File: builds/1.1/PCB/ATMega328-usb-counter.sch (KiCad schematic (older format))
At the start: 38 parts, among them J1 power, J2 PROG, J3 USB_B_Micro, J4 RF, J5 PROG, Q1 MMBT3904, U1 FT230XS, U2 ATmega328PB-AU, U3 74LV8154, X1 TCXO

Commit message: rev 1.1 PCB
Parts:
- added H1, H2, H3: MountingHole, MountingHole:MountingHole_4.3mm_M4_Pad_Via, symbol Mechanical:MountingHole
- J3: footprint (none) -> Connector_USB:USB_Micro-B_Molex-105017-0001
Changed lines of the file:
@@
 F 0 "J3" H 1307 2267 50  0000 C CNN
 F 1 "USB_B_Micro" H 1307 2176 50  0000 C CNN
-F 2 "" H 1400 1750 50  0001 C CNN
+F 2 "Connector_USB:USB_Micro-B_Molex-105017-0001" H 1400 1750 50  0001 C CNN
 F 3 "~" H 1400 1750 50  0001 C CNN
 	1    1250 1800
@@
 Text Notes 9700 850  0    98   ~ 0
 LCD
+$Comp
+L Mechanical:MountingHole H1
+U 1 1 5D44527F
+P 10050 2550
+F 0 "H1" H 10150 2596 50  0000 L CNN
+F 1 "MountingHole" H 10150 2505 50  0000 L CNN
+F 2 "MountingHole:MountingHole_4.3mm_M4_Pad_Via" H 10050 2550 50  0001 C CNN
+F 3 "~" H 10050 2550 50  0001 C CNN
+	1    10050 2550
+	1    0    0    -1
+$EndComp
+$Comp
+L Mechanical:MountingHole H2
+U 1 1 5D4460C1
+P 10050 2850
+F 0 "H2" H 10150 2896 50  0000 L CNN
+F 1 "MountingHole" H 10150 2805 50  0000 L CNN
+F 2 "MountingHole:MountingHole_4.3mm_M4_Pad_Via" H 10050 2850 50  0001 C CNN
+F 3 "~" H 10050 2850 50  0001 C CNN
+	1    10050 2850
+	1    0    0    -1
+$EndComp
+$Comp
+L Mechanical:MountingHole H3
+U 1 1 5D463B97
+P 10050 3150
+F 0 "H3" H 10150 3196 50  0000 L CNN
+F 1 "MountingHole" H 10150 3105 50  0000 L CNN
+F 2 "MountingHole:MountingHole_4.3mm_M4_Pad_Via" H 10050 3150 50  0001 C CNN
+F 3 "~" H 10050 3150 50  0001 C CNN
+	1    10050 3150
+	1    0    0    -1
+$EndComp
 $EndSCHEMATC

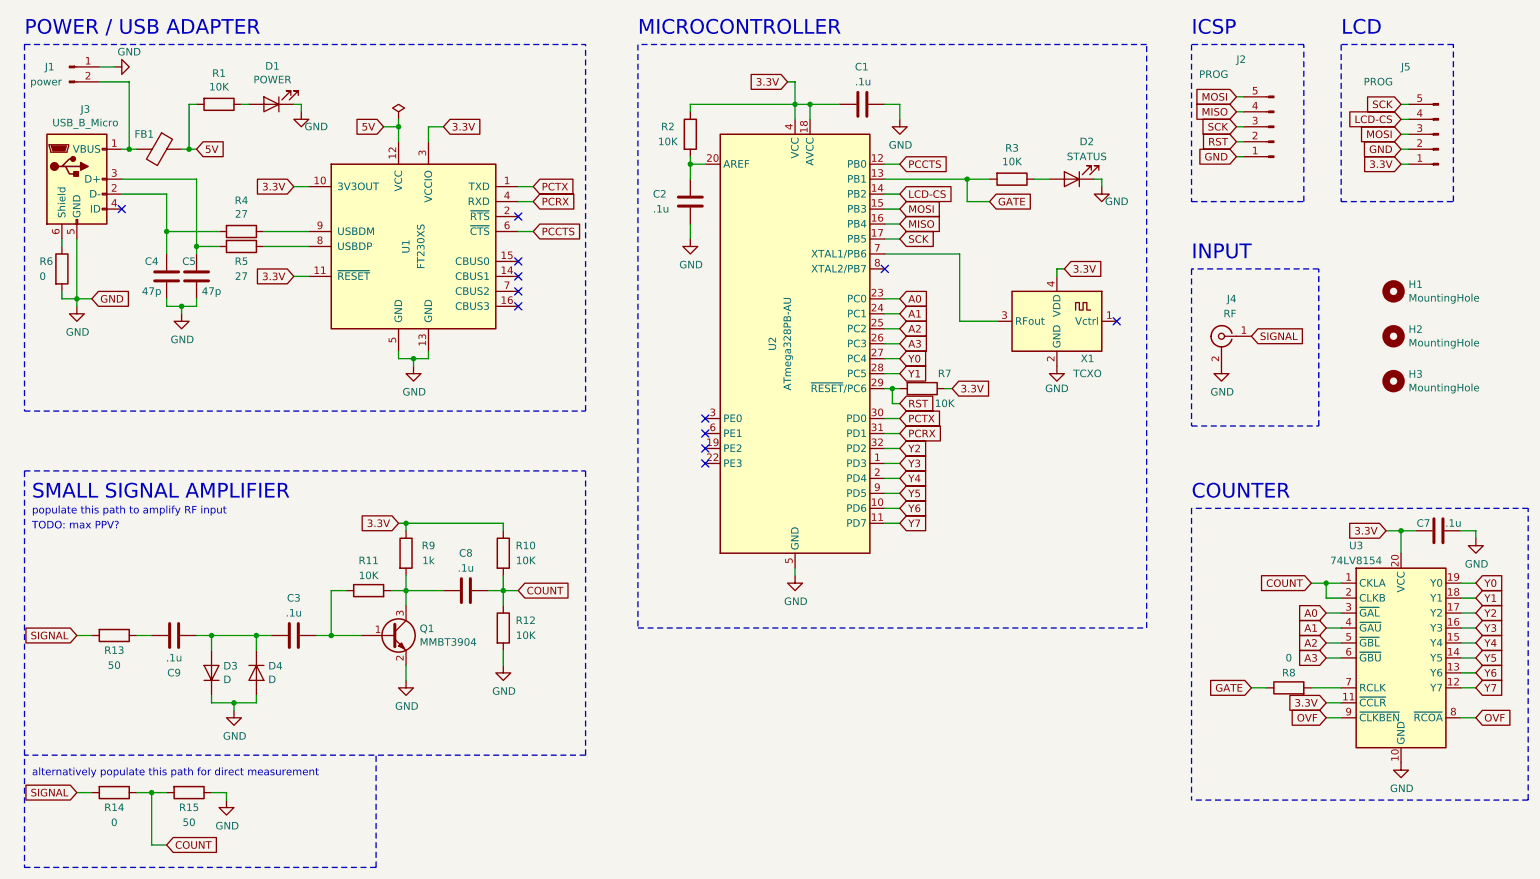
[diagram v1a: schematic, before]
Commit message: added screw hole
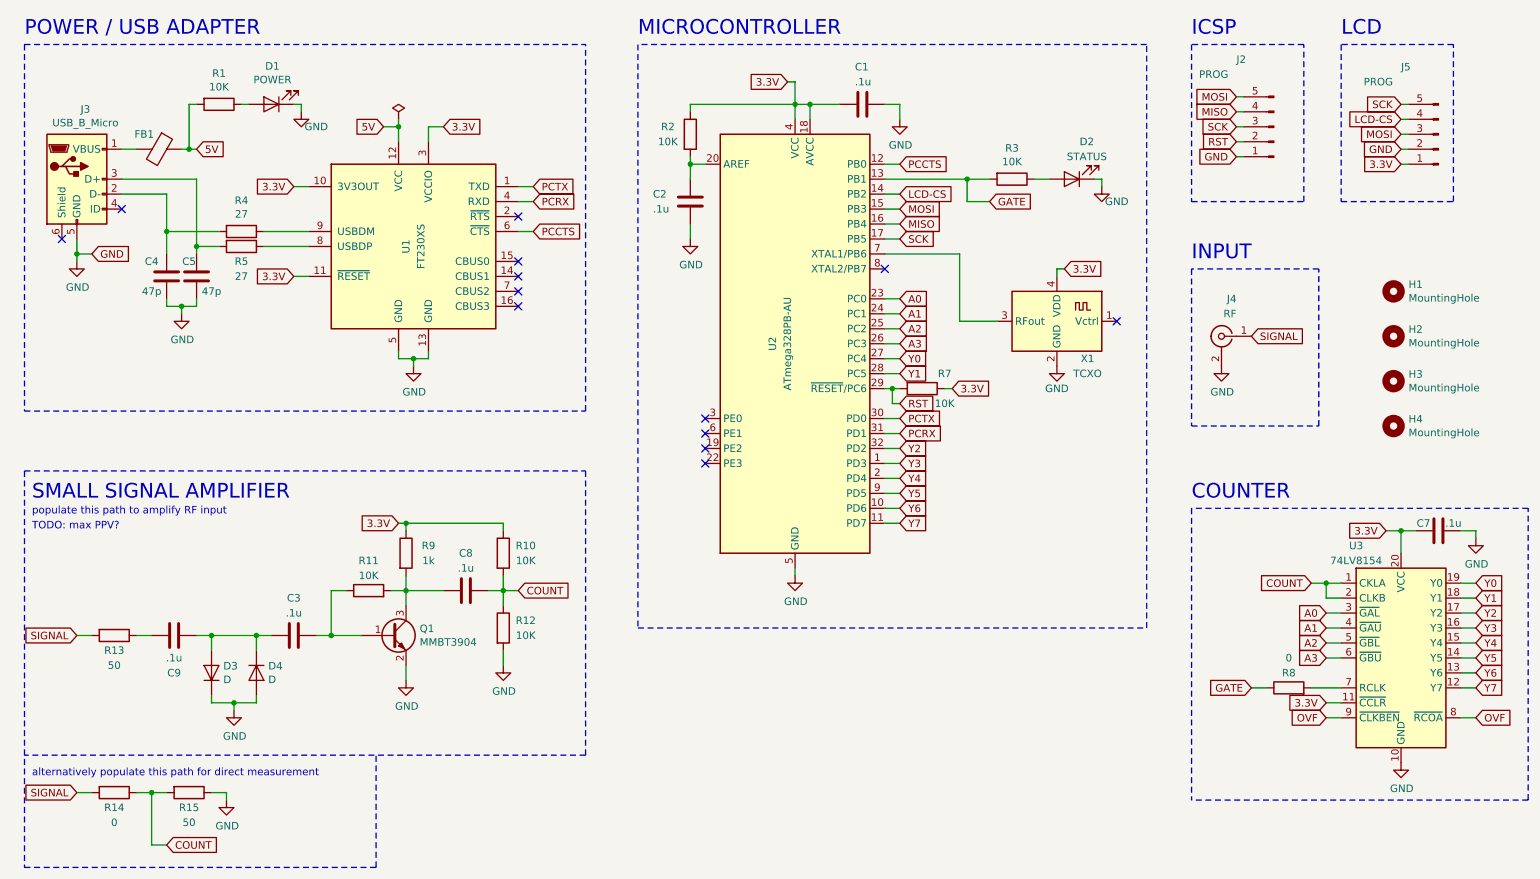
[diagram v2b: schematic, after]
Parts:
- removed J1: power, Connector_PinHeader_2.54mm:PinHeader_1x02_P2.54mm_Vertical, symbol Connector:Conn_01x02_Male
- removed R6: 0, Resistor_SMD:R_0805_2012Metric_Pad1.15x1.40mm_HandSolder, symbol Device:R
- added H4: MountingHole, MountingHole:MountingHole_4.3mm_M4_Pad_Via, symbol Mechanical:MountingHole
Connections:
- no-connect marks 12 -> 13
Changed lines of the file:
@@
 L power:GND #PWR08
 U 1 1 5CDBD712
-P 1250 2650
-F 0 "#PWR08" H 1250 2400 50  0001 C CNN
-F 1 "GND" H 1255 2477 50  0000 C CNN
-F 2 "" H 1250 2650 50  0001 C CNN
-F 3 "" H 1250 2650 50  0001 C CNN
-	1    1250 2650
-	1    0    0    -1
-$EndComp
-Wire Wire Line
-	1150 2200 1150 2250
-Wire Wire Line
-	1150 2550 1150 2600
-Wire Wire Line
-	1250 2600 1250 2200
-Wire Wire Line
-	1150 2600 1250 2600
-Wire Wire Line
-	1250 2600 1250 2650
-Connection ~ 1250 2600
+P 1250 2350
+F 0 "#PWR08" H 1250 2100 50  0001 C CNN
+F 1 "GND" H 1255 2177 50  0000 C CNN
+F 2 "" H 1250 2350 50  0001 C CNN
+F 3 "" H 1250 2350 50  0001 C CNN
+	1    1250 2350
+	1    0    0    -1
+$EndComp
+Wire Wire Line
+	1250 2300 1250 2350
 Wire Wire Line
 	2050 2250 2200 2250
@@
 	1950 2650 2050 2650
 $Comp
-L Device:R R6
-U 1 1 5CDD40A1
-P 1150 2400
-F 0 "R6" H 1000 2450 50  0000 L CNN
-F 1 "0" H 1000 2350 50  0000 L CNN
-F 2 "Resistor_SMD:R_0805_2012Metric_Pad1.15x1.40mm_HandSolder" V 1080 2400 50  0001 C CNN
-F 3 "~" H 1150 2400 50  0001 C CNN
-	1    1150 2400
-	1    0    0    -1
-$EndComp
-$Comp
 L Device:R R4
 U 1 1 5CE26301
@@
 Wire Wire Line
 	2750 1350 2750 1300
-Wire Wire Line
-	1600 1600 1550 1600
-Connection ~ 1600 1600
 Text GLabel 2050 1600 2    50   Input ~ 0
 5V
 Wire Wire Line
 	1950 1600 2000 1600
-Wire Wire Line
-	1650 1600 1600 1600
 $Comp
 L power:GND #PWR02
@@
 Wire Wire Line
 	6750 4000 6650 4000
-$Comp
-L Connector:Conn_01x02_Male J1
-U 1 1 5D39A20E
-P 1200 1050
-F 0 "J1" H 1100 1050 50  0000 R CNN
-F 1 "power" H 1150 950 50  0000 R CNN
-F 2 "Connector_PinHeader_2.54mm:PinHeader_1x02_P2.54mm_Vertical" H 1200 1050 50  0001 C CNN
-F 3 "~" H 1200 1050 50  0001 C CNN
-	1    1200 1050
-	1    0    0    -1
-$EndComp
 Text GLabel 7350 1950 2    50   Input ~ 0
 GATE
@@
 	1    0    0    -1
 $EndComp
-Wire Wire Line
-	1600 1150 1400 1150
-$Comp
-L power:GND #PWR01
-U 1 1 5D23D013
-P 1500 1050
-F 0 "#PWR01" H 1500 800 50  0001 C CNN
-F 1 "GND" V 1600 950 50  0000 C CNN
-F 2 "" H 1500 1050 50  0001 C CNN
-F 3 "" H 1500 1050 50  0001 C CNN
-	1    1500 1050
-	0    -1   -1   0
-$EndComp
-Wire Wire Line
-	1500 1050 1400 1050
 Text GLabel 6750 1700 2    50   Input ~ 0
 PCCTS
@@
 	1    0    0    -1
 $EndComp
-Wire Wire Line
-	1600 1150 1600 1600
 Wire Wire Line
 	2050 1300 2000 1300
@@
 Wire Notes Line
 	8400 4800 8400 900
-Text GLabel 1350 2600 2    50   Input ~ 0
+Text GLabel 1350 2300 2    50   Input ~ 0
 GND
 Wire Wire Line
-	1350 2600 1250 2600
+	1350 2300 1250 2300
 Text GLabel 9000 1650 0    50   Input ~ 0
 GND
@@
 	1    0    0    -1
 $EndComp
+$Comp
+L Mechanical:MountingHole H4
+U 1 1 5D3E5B2C
+P 10050 3450
+F 0 "H4" H 10150 3496 50  0000 L CNN
+F 1 "MountingHole" H 10150 3405 50  0000 L CNN
+F 2 "MountingHole:MountingHole_4.3mm_M4_Pad_Via" H 10050 3450 50  0001 C CNN
+F 3 "~" H 10050 3450 50  0001 C CNN
+	1    10050 3450
+	1    0    0    -1
+$EndComp
+Wire Wire Line
+	1550 1600 1650 1600
+Wire Wire Line
+	1250 2300 1250 2200
+Connection ~ 1250 2300
+NoConn ~ 1150 2200
 $EndSCHEMATC

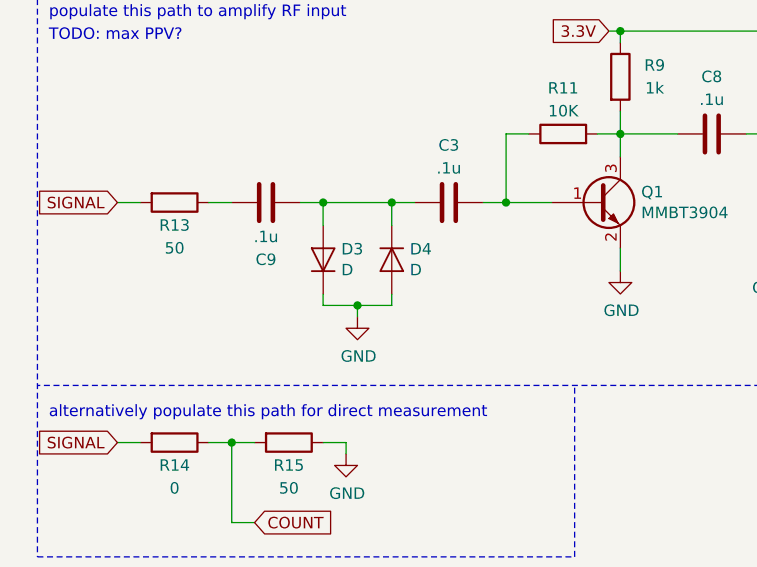
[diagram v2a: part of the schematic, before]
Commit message: new diode protection
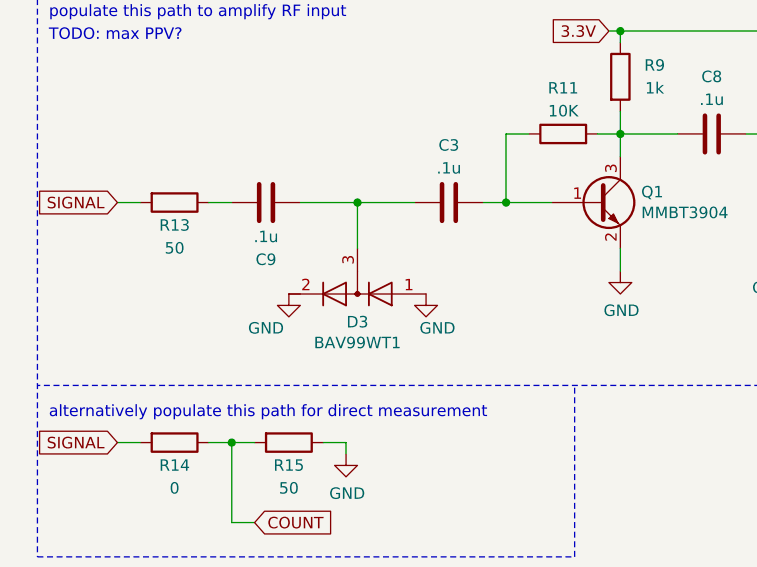
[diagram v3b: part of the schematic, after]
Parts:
- removed D3, D4: D, Diode_SMD:D_0805_2012Metric_Pad1.15x1.40mm_HandSolder, symbol Device:D
- added D3: BAV99WT1, Package_TO_SOT_SMD:SOT-323_SC-70_Handsoldering, symbol Device:D_x2_Serial_AKC
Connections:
- net GND: now also D3.1 (A), D3.2 (K)
- net at C3.2, C9.2: now also D3.3 (common)
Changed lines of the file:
@@
 	1250 4850 1350 4850
-$Comp
-L Device:D D3
-U 1 1 5D5548F3
-P 2150 5100
-F 0 "D3" V 2196 5021 50  0000 R CNN
-F 1 "D" V 2105 5021 50  0000 R CNN
-F 2 "Diode_SMD:D_0805_2012Metric_Pad1.15x1.40mm_HandSolder" H 2150 5100 50  0001 C CNN
-F 3 "~" H 2150 5100 50  0001 C CNN
-	1    2150 5100
-	0    -1   -1   0
-$EndComp
-$Comp
-L Device:D D4
-U 1 1 5D555473
-P 2450 5100
-F 0 "D4" V 2404 5179 50  0000 L CNN
-F 1 "D" V 2495 5179 50  0000 L CNN
-F 2 "Diode_SMD:D_0805_2012Metric_Pad1.15x1.40mm_HandSolder" H 2450 5100 50  0001 C CNN
-F 3 "~" H 2450 5100 50  0001 C CNN
-	1    2450 5100
-	0    1    1    0
-$EndComp
-$Comp
-L power:GND #PWR017
-U 1 1 5D5A15B6
-P 2300 5350
-F 0 "#PWR017" H 2300 5100 50  0001 C CNN
-F 1 "GND" H 2305 5177 50  0000 C CNN
-F 2 "" H 2300 5350 50  0001 C CNN
-F 3 "" H 2300 5350 50  0001 C CNN
-	1    2300 5350
-	1    0    0    -1
-$EndComp
-Wire Wire Line
-	2150 5300 2300 5300
-Wire Wire Line
-	2150 5300 2150 5250
-Wire Wire Line
-	2300 5300 2450 5300
-Connection ~ 2300 5300
-Wire Wire Line
-	2300 5350 2300 5300
-Wire Wire Line
-	2450 5300 2450 5250
 $Comp
 L Transistor_BJT:MMBT3904 Q1
@@
 	1    0    0    -1
 $EndComp
-Wire Wire Line
-	2450 4950 2450 4850
-Wire Wire Line
-	2450 4850 2150 4850
-Wire Wire Line
-	2150 4950 2150 4850
-Connection ~ 2150 4850
-Wire Wire Line
-	2150 4850 2050 4850
 $Comp
 L Device:C C3
@@
 	0    1    1    0
 $EndComp
-Wire Wire Line
-	2550 4850 2450 4850
-Connection ~ 2450 4850
 Wire Wire Line
 	3050 4550 2950 4550
@@
 Connection ~ 1250 2300
 NoConn ~ 1150 2200
+Wire Wire Line
+	2050 4850 2300 4850
+$Comp
+L power:GND #PWR017
+U 1 1 5D5A15B6
+P 2000 5250
+F 0 "#PWR017" H 2000 5000 50  0001 C CNN
+F 1 "GND" H 1900 5100 50  0000 C CNN
+F 2 "" H 2000 5250 50  0001 C CNN
+F 3 "" H 2000 5250 50  0001 C CNN
+	1    2000 5250
+	1    0    0    -1
+$EndComp
+$Comp
+L power:GND #PWR01
+U 1 1 5D3F2AE8
+P 2600 5250
+F 0 "#PWR01" H 2600 5000 50  0001 C CNN
+F 1 "GND" H 2650 5100 50  0000 C CNN
+F 2 "" H 2600 5250 50  0001 C CNN
+F 3 "" H 2600 5250 50  0001 C CNN
+	1    2600 5250
+	1    0    0    -1
+$EndComp
+Connection ~ 2300 4850
+Wire Wire Line
+	2300 4850 2550 4850
+Wire Wire Line
+	2300 4850 2300 5050
+$Comp
+L Device:D_x2_Serial_AKC D3
+U 1 1 5D3E819A
+P 2300 5250
+F 0 "D3" H 2300 5373 50  0000 C CNN
+F 1 "BAV99WT1" H 2300 5464 50  0000 C CNN
+F 2 "Package_TO_SOT_SMD:SOT-323_SC-70_Handsoldering" H 2300 5250 50  0001 C CNN
+F 3 "~" H 2300 5250 50  0001 C CNN
+	1    2300 5250
+	-1   0    0    1
+$EndComp
 $EndSCHEMATC
